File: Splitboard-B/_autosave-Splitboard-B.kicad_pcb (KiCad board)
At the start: 2 copper layers, 185 x 158.7 mm, 83 parts, among them J1 USB_C_Receptacle, K1 KEYSW, K10 KEYSW, K11 KEYSW, K12 KEYSW, K13 KEYSW, K14 KEYSW, K15 KEYSW, K16 KEYSW, K17 KEYSW, K18 KEYSW, K19 KEYSW, K2 KEYSW, K20 KEYSW, K21 KEYSW, K22 KEYSW, K23 KEYSW, K24 KEYSW, K25 KEYSW, K26 KEYSW, K27 KEYSW, K28 KEYSW, K29 KEYSW, K3 KEYSW, K30 KEYSW, K31 KEYSW, K32 KEYSW, K33 KEYSW, K34 KEYSW, K35 KEYSW, K36 KEYSW, K37 KEYSW, K38 KEYSW, K4 KEYSW, K5 KEYSW, K6 KEYSW, K7 KEYSW, K8 KEYSW, K9 KEYSW, SW1 RotaryEncoder, U3 CR2013-MI2120

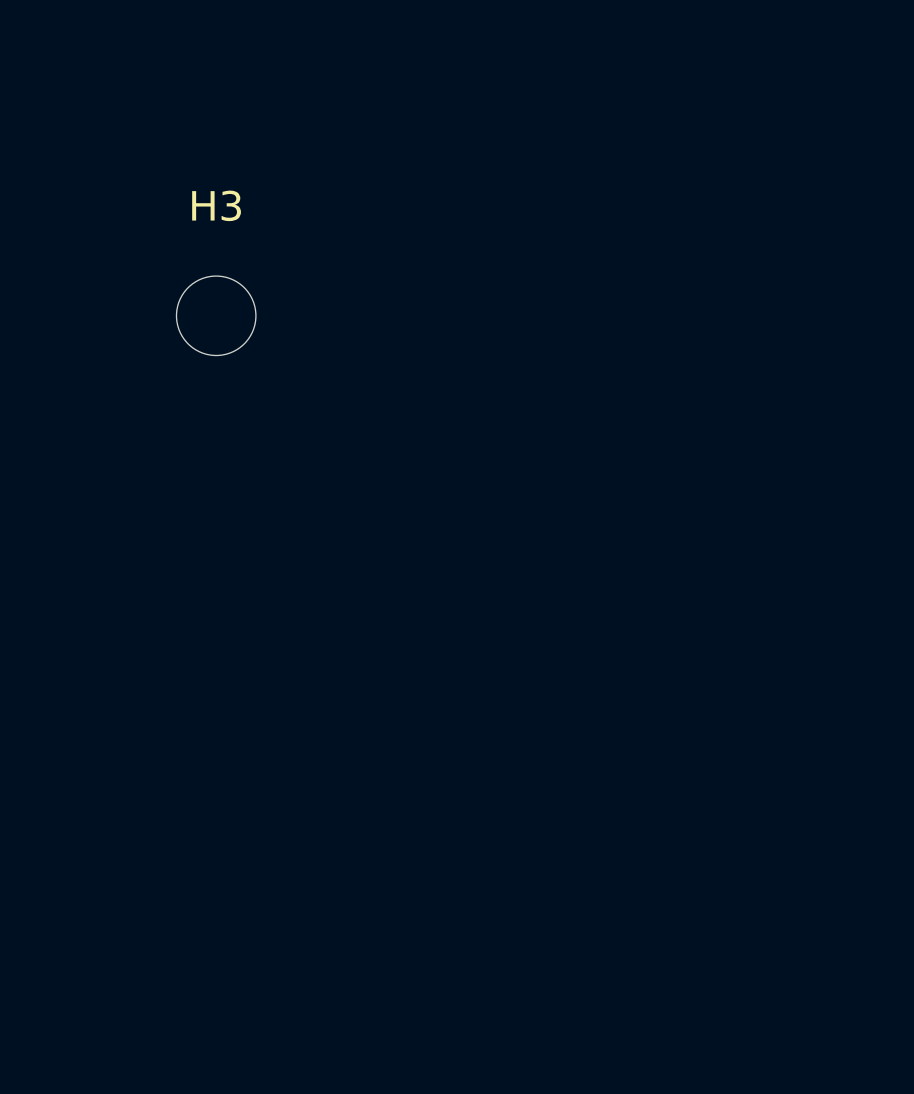
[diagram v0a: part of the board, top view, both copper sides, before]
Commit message: created 3d model for the keyboard as well as kbt1 acrylic models
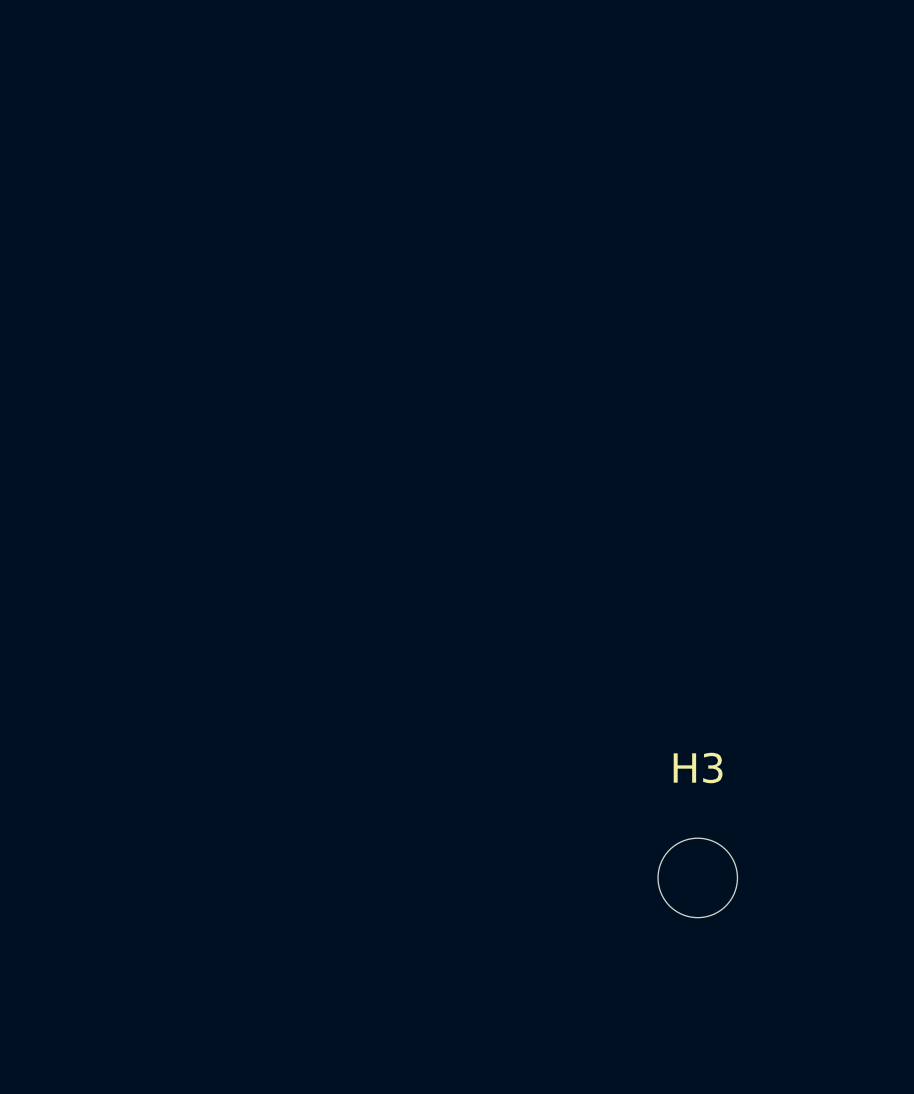
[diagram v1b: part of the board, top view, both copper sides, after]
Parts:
- moved H3 25.2 mm to (149.9, 205.7)
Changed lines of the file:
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@@
   )
   (footprint "MountingHole:MountingHole_2.7mm" (layer "F.Cu")
-    (at 133.49 186.63)
+    (at 149.86 205.74)
     (descr "Mounting Hole 2.7mm, no annular")
     (tags "mounting hole 2.7mm no annular")
